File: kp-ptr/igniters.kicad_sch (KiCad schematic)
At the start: 44 parts, among them J10 Conn_01x02, J11 Conn_01x02, J12 Conn_01x02, J13 Conn_01x02, Q2 DMC2025UFDB_v2, Q3 DMC2025UFDB_v2, Q4 DMC2025UFDB_v2, Q5 DMC2025UFDB_v2

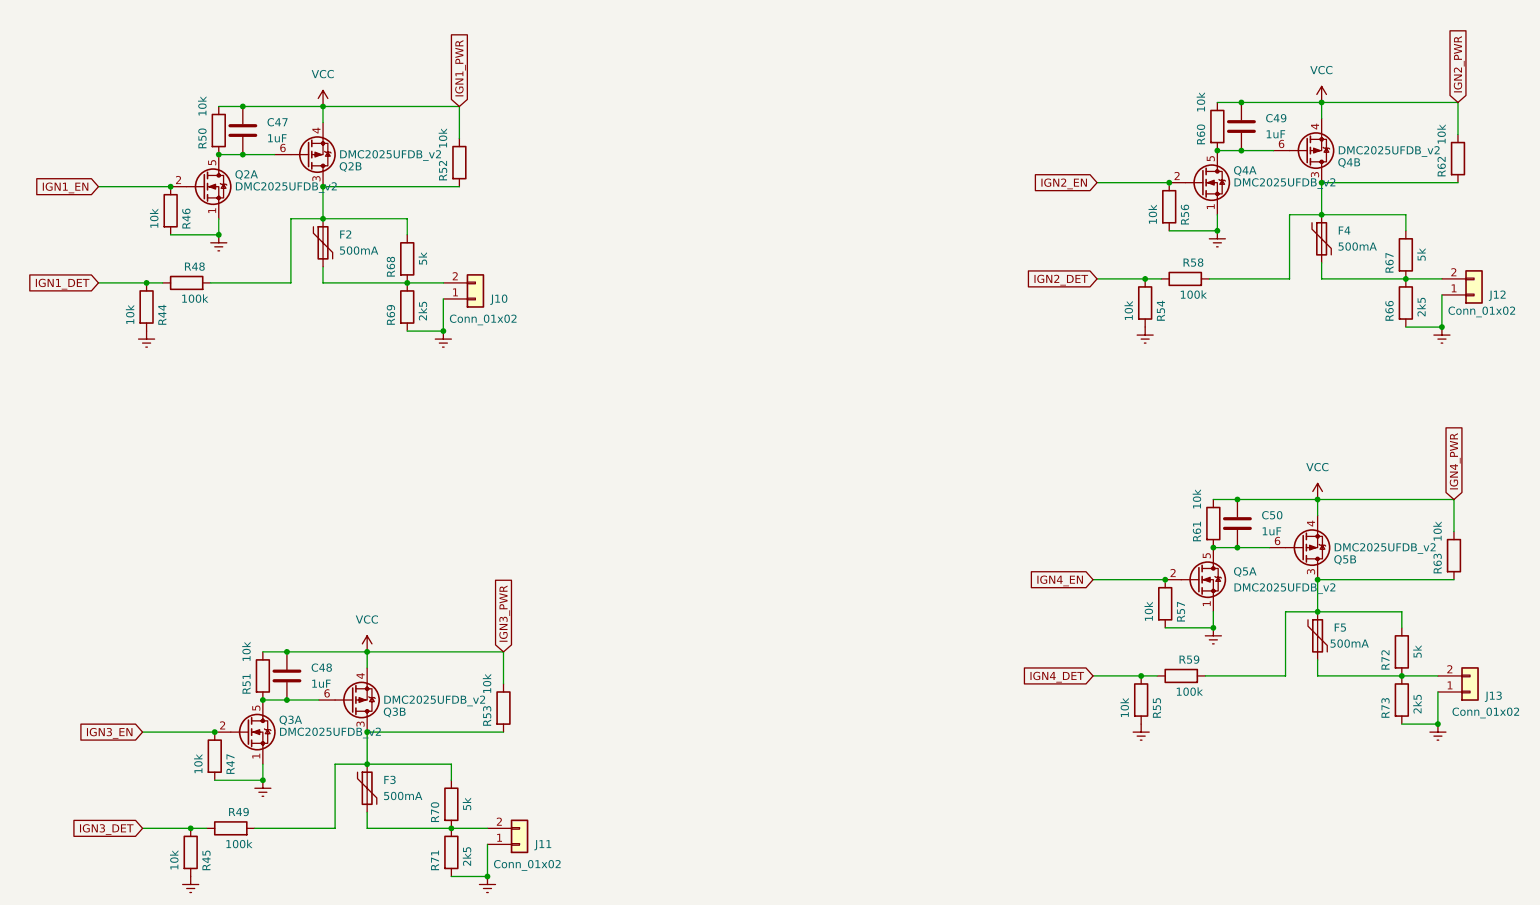
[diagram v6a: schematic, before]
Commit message: Igniters rework
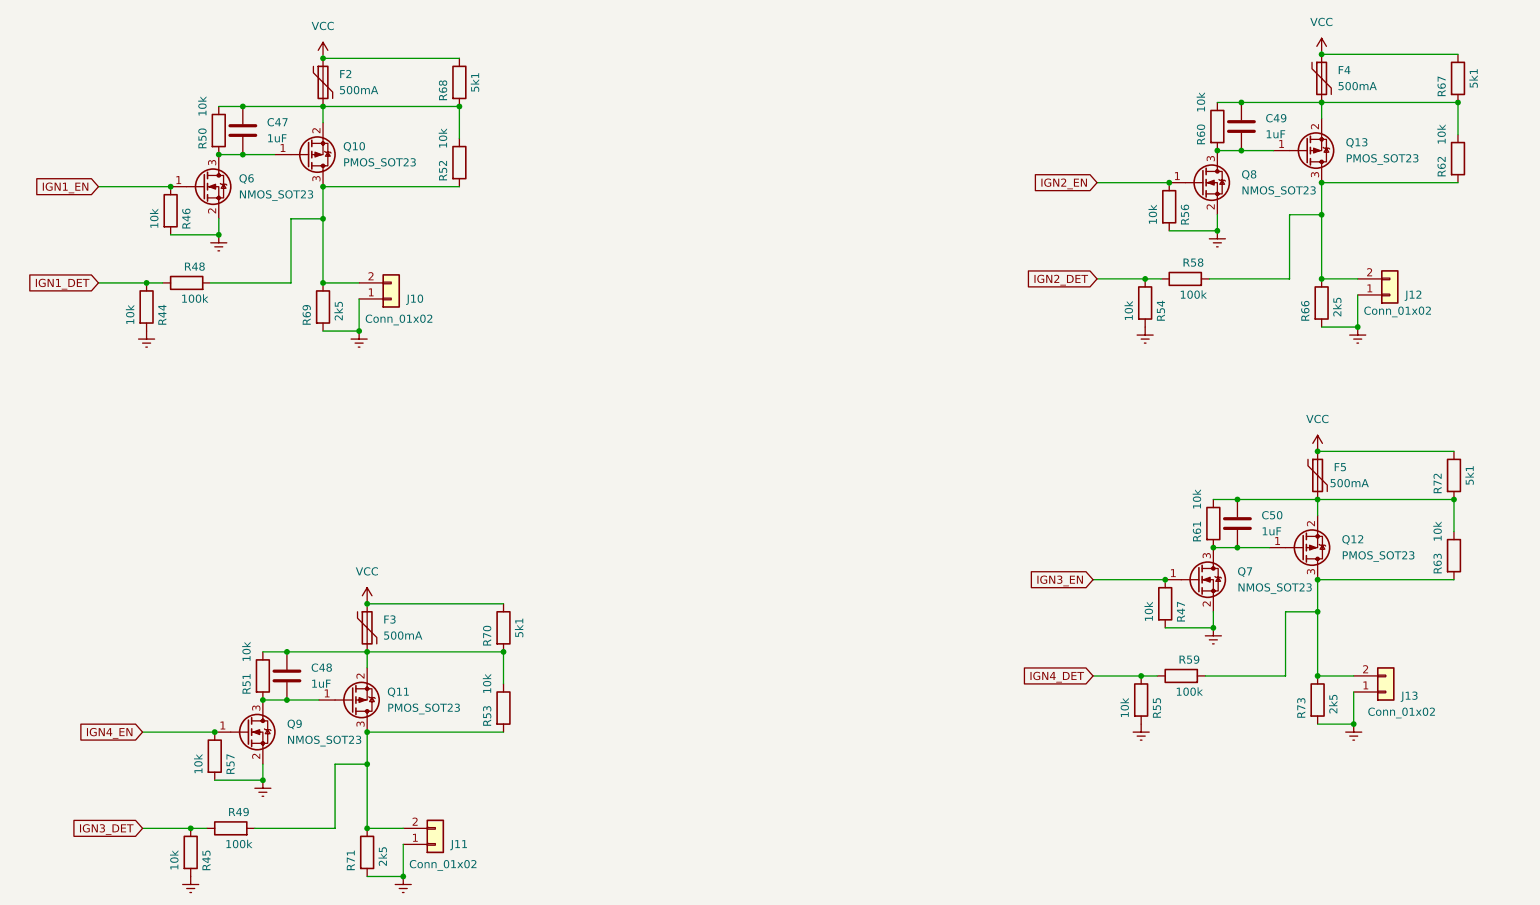
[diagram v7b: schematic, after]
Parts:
- removed Q2, Q3, Q4, Q5: DMC2025UFDB_v2, KP-PTR_lib:DMC2025UFDB, symbol KP-PTR_lib:DMC2025UFDB_v2
- added Q10, Q11, Q12, Q13: PMOS_SOT23, KP-PTR_lib:SOT-23, symbol Transistor_FET:IRLML6401
- added Q6, Q7, Q8, Q9: NMOS_SOT23, KP-PTR_lib:SOT-23, symbol Transistor_FET:IRLML2060
- R67, R68, R70, R72: value 5k -> 5k1
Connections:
- net Earth: now also Q6.2 (S), Q7.2 (S), Q8.2 (S), Q9.2 (S)
- net IGN1_EN: now also Q6.1 (G)
- net IGN2_EN: now also Q8.1 (G)
- net IGN3_EN: now also Q7.1 (G)
- net IGN4_EN: now also Q9.1 (G)
- net VCC: now also F2.1, F3.1, F4.1, F5.1, R67.1, R68.1, R70.1, R72.1; no longer C47.1, C48.1, C49.1, C50.1, R50.1, R51.1, R52.1, R53.1, R60.1, R61.1, R62.1, R63.1
- net at R49.2, R53.2: now also J11.2 (Pin_2), R71.1, Q11.3 (D); no longer F3.1, R70.1
- net at C48.2, R51.2: now also Q11.1 (G), Q9.3 (D)
- net at R59.2, R63.2: now also J13.2 (Pin_2), R73.1, Q12.3 (D); no longer F5.1, R72.1
- net at C50.2, R61.2: now also Q12.1 (G), Q7.3 (D)
- net at F5.2, R72.2: now also C50.1, R61.1, R63.1, Q12.2 (S); no longer J13.2 (Pin_2), R73.1
- net at R48.2, R52.2: now also J10.2 (Pin_2), R69.1, Q10.3 (D); no longer F2.1, R68.1
- net at C47.2, R50.2: now also Q10.1 (G), Q6.3 (D)
- net at F3.2, R70.2: now also C48.1, R51.1, R53.1, Q11.2 (S); no longer J11.2 (Pin_2), R71.1
- net at F2.2, R68.2: now also C47.1, R50.1, R52.1, Q10.2 (S); no longer J10.2 (Pin_2), R69.1
- net at C49.2, R60.2: now also Q13.1 (G), Q8.3 (D)
- net at F4.2, R67.2: now also C49.1, R60.1, R62.1, Q13.2 (S); no longer J12.2 (Pin_2), R66.1
- net at R58.2, R62.2: now also J12.2 (Pin_2), R66.1, Q13.3 (D); no longer F4.1, R67.1
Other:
- moved on the sheet: F2, F3, F4, F5, J10, J11, J12, J13, R47, R57, R66, R67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

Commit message: Igniters rework v2
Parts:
- added Q2, Q3, Q4, Q5: PMOS_SOT23, KP-PTR_lib:SOT-23, symbol Transistor_FET:IRLML6401
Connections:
- net VCC: now also C47.1, C48.1, C49.1, C50.1, Q10.2 (S), Q11.2 (S), Q12.2 (S), Q13.2 (S), R50.1, R51.1, R52.1, R53.1, R60.1, R61.1, R62.1, R63.1, Q2.2 (S), Q3.2 (S), Q4.2 (S), Q5.2 (S); no longer F2.1, F3.1, F4.1, F5.1, R67.1, R68.1, R70.1, R72.1
- net at C50.2, Q12.1 (G), Q7.3 (D)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: now also Q4.1 (G)
- net at Q12.3 (D), R59.2, R63.2: now also F5.1, R72.1, Q4.3 (D); no longer J13.2 (Pin_2), R73.1
- net at Q11.3 (D), R49.2, R53.2: now also F3.1, R70.1, Q2.3 (D); no longer J11.2 (Pin_2), R71.1
- net at Q10.3 (D), R48.2, R52.2: now also F2.1, R68.1, Q3.3 (D); no longer J10.2 (Pin_2), R69.1
- net at C49.2, Q13.1 (G), Q8.3 (D)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: now also Q5.1 (G)
- net at Q13.3 (D), R58.2, R62.2: now also F4.1, R67.1, Q5.3 (D); no longer J12.2 (Pin_2), R66.1
- net at C47.2, Q10.1 (G), Q6.3 (D)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: now also Q3.1 (G)
- net at C48.2, Q11.1 (G), Q9.3 (D)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: now also Q2.1 (G)
- new net: F5.2, J13.2 (Pin_2), R72.2, R73.1
- new net: F3.2, J11.2 (Pin_2), R70.2, R71.1
- new net: F2.2, J10.2 (Pin_2), R68.2, R69.1
- new net: F4.2, J12.2 (Pin_2), R66.1, R67.2
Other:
- moved on the sheet: C48, C49, C50, F2, F3, F4, F5, J10, J11, J12, J13, Q11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
